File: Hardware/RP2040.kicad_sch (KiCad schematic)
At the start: 41 parts, among them J24 USB_C_Receptacle_USB2.0_14P, SW2 SW_Push_Dual, U1 W25Q128JVS, U2 RP2040, Y1 ABM8-272-T3

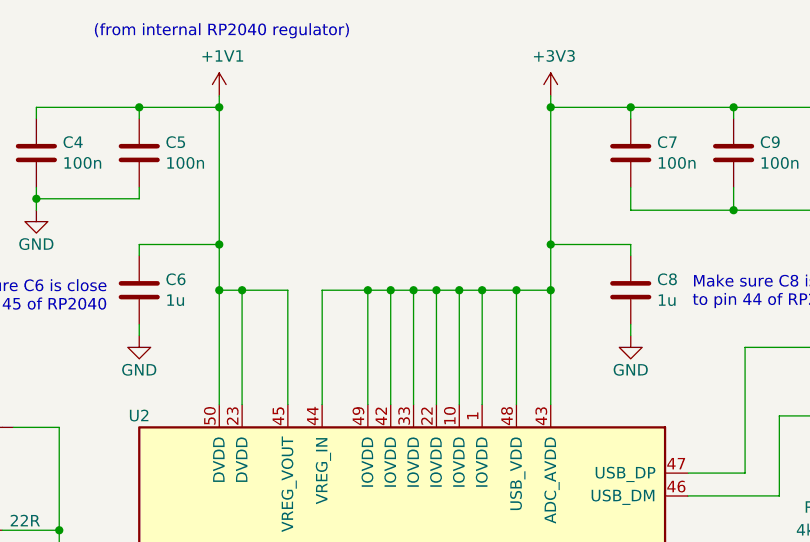
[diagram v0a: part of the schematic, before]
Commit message: Place RP2040
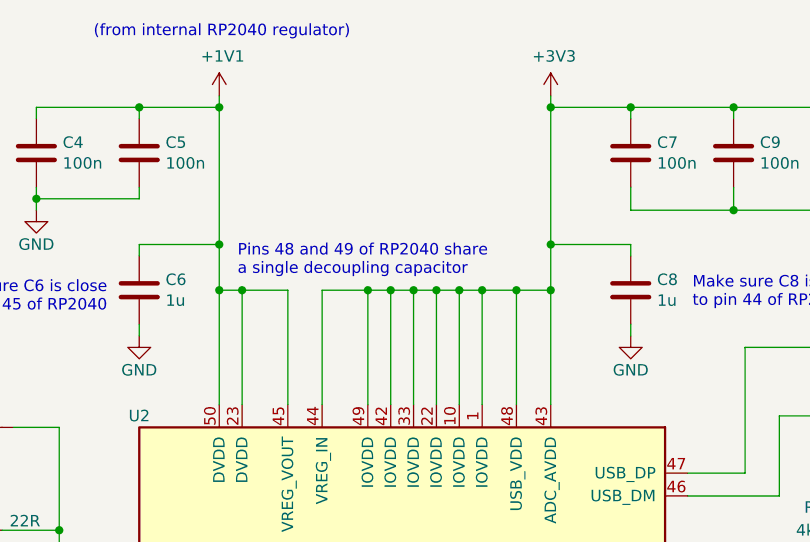
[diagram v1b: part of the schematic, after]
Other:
- note added: "Pins 48 and 49 of RP2040 share a single decoupling capacitor"
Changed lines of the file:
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@@
+		)
+	)
+	(text "Pins 48 and 49 of RP2040 share\na single decoupling capacitor"
+		(exclude_from_sim no)
+		(at 188.722 81.026 0)
+		(effects
+			(font
+				(size 1.27 1.27)
+			)
+			(justify left bottom)
 		)
 	)

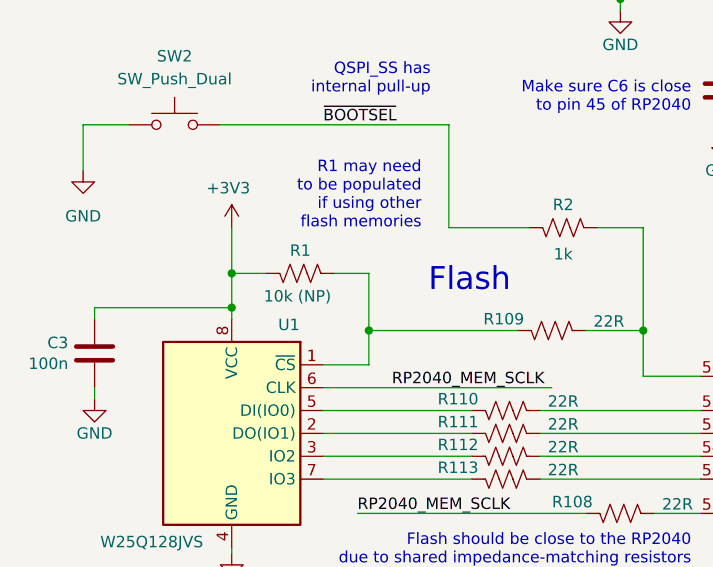
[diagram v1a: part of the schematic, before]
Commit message: MPI layout
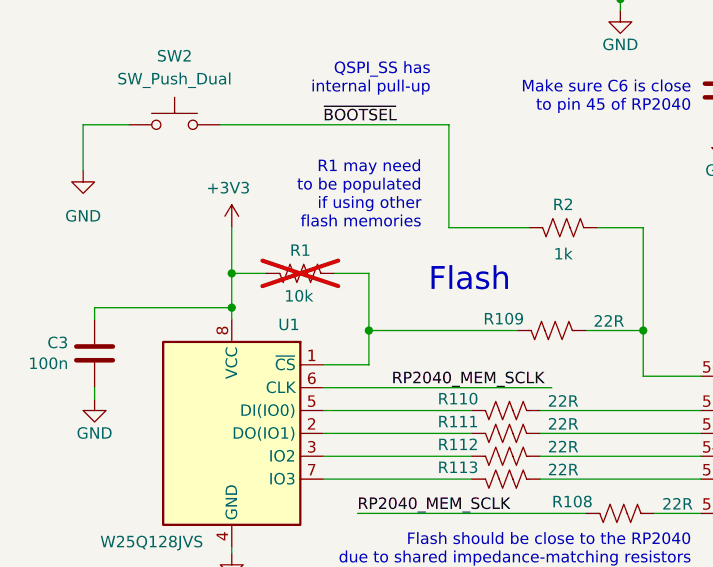
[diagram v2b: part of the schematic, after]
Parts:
- R1: value 10k (NP) -> 10k; now not fitted
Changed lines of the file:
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@@
 		(in_bom yes)
 		(on_board yes)
-		(dnp no)
+		(dnp yes)
 		(property "Reference" "R1"
 			(at 130.81 100.33 90)
@@
 			)
 		)
-		(property "Value" "10k (NP)"
-			(at 126.746 105.41 90)
+		(property "Value" "10k"
+			(at 129.032 105.41 90)
 			(effects
 				(font
